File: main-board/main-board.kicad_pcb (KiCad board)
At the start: 2 copper layers, 180 x 111 mm, 57 parts, among them J1 INPUT, J2 NC1, J3 OUTPUT, J4 Conn_01x03_Pin, J5 COM, J6 Conn_01x03_Pin, SW1 SW_SPST, U1 ADA4898-2, U2 ADA4898-2, U3 AD633ANZ

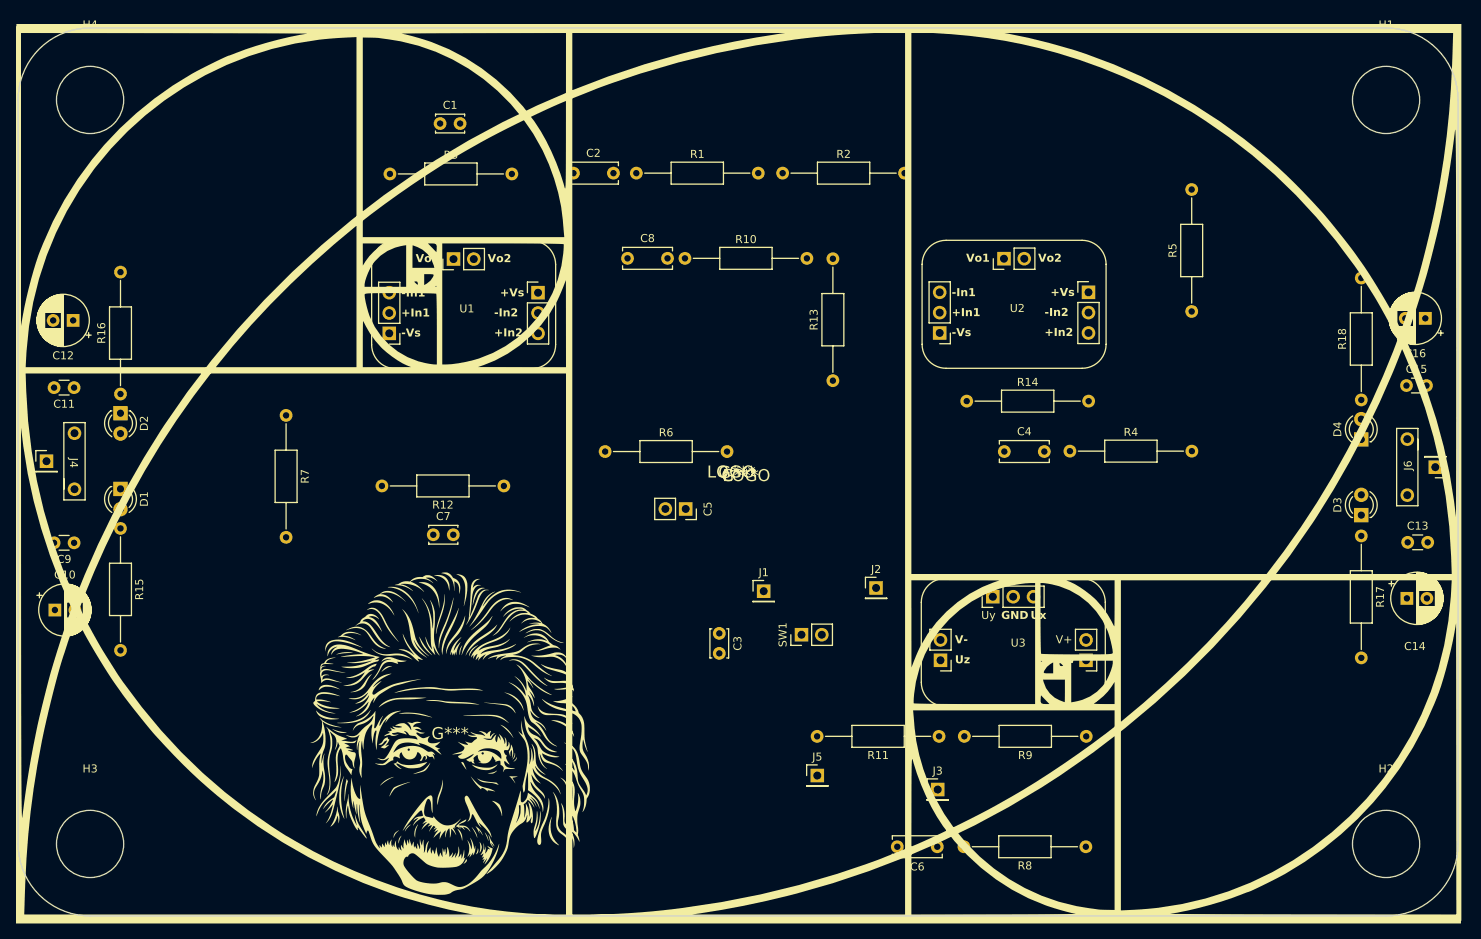
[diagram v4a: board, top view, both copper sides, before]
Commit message: Modifies main board layout components displacement
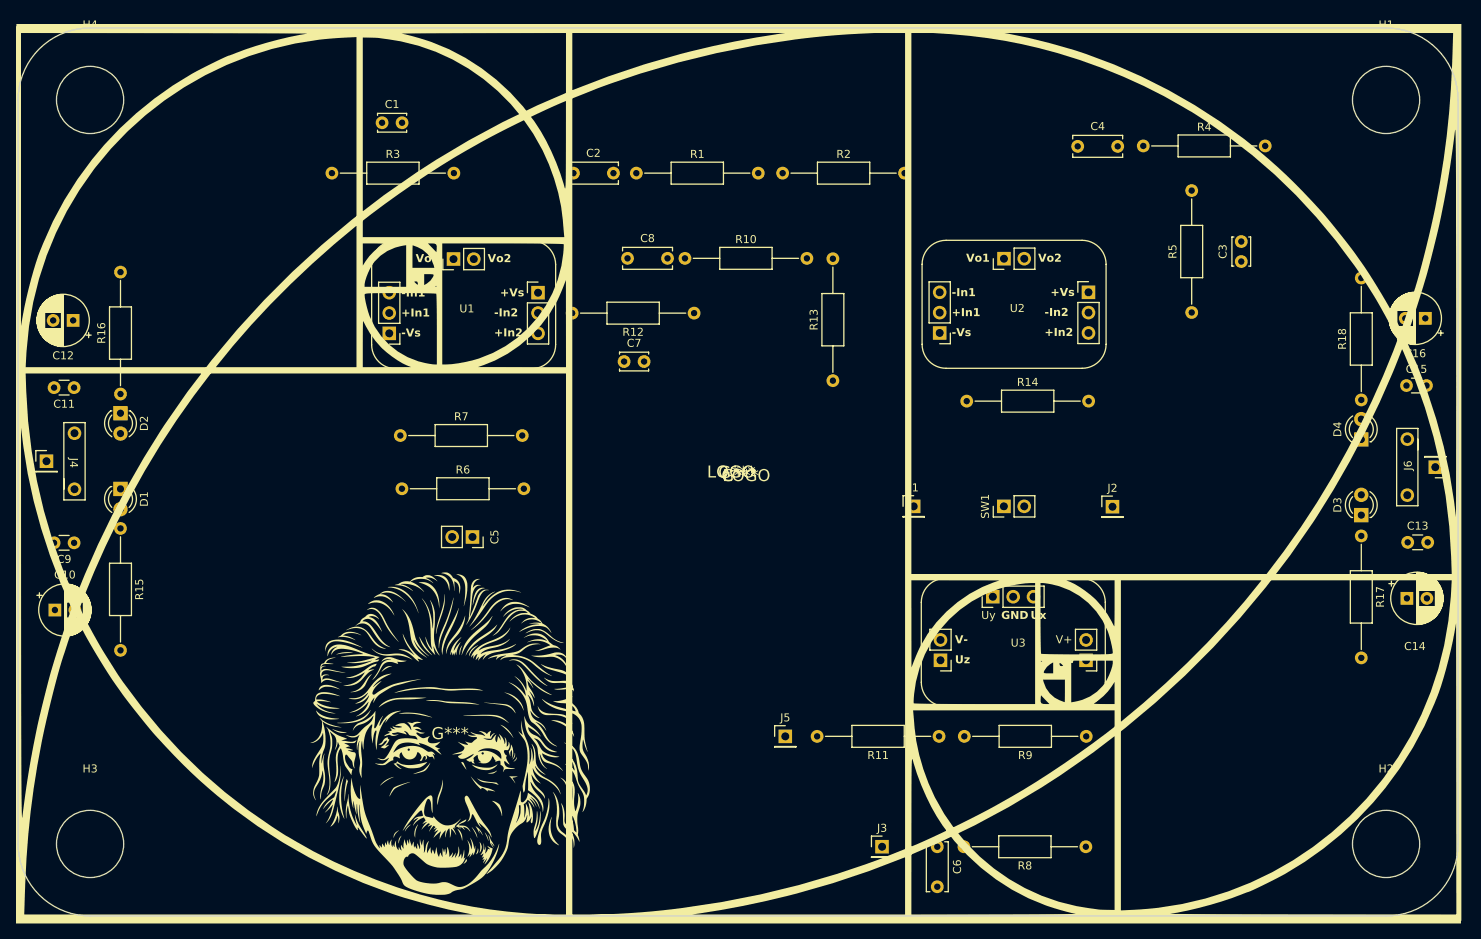
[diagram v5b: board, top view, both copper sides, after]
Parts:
- moved C3 80.1 mm to (212.9, 72.2), turned to 90 degrees
- moved R4 39.2 mm to (200.7, 57.8)
- moved C4 39.2 mm to (192.4, 57.8)
- moved C7 32.2 mm to (135.8, 84.7)
- moved R12 32.1 mm to (144.5, 78.7)
- moved J2 31.2 mm to (196.8, 102.8)
- moved SW1 30.0 mm to (183.2, 102.8)
- moved C5 26.9 mm to (116.8, 106.6)
- moved R6 25.8 mm to (108.0, 100.6)
- moved J1 21.5 mm to (171.9, 102.8)
- moved R7 14.5 mm to (107.8, 94.0), turned to 0 degrees
- moved J3 9.97 mm to (168.0, 145.3)
- moved C1 7.25 mm to (105.5, 54.9)
- moved R3 7.25 mm to (99.2, 61.1)
- moved J5 6.33 mm to (155.9, 131.6)
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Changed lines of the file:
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@@
   )
   (footprint "footprints:Switch" (layer "F.Cu")
-    (at 157.925 118.85 90)
+    (at 183.225 102.8 90)
     (property "Sheetfile" "main-board.kicad_sch")
     (property "Sheetname" "")
@@
   )
   (footprint "Capacitor_THT:C_Disc_D6.0mm_W2.5mm_P5.00mm" (layer "F.Cu")
-    (at 183.28 95.95)
+    (at 192.45 57.8)
     (descr "C, Disc series, Radial, pin pitch=5.00mm, , diameter*width=6*2.5mm^2, Capacitor, http://cdn-reichelt.de/documents/datenblatt/B300/DS_KERKO_TC.pdf")
     (tags "C Disc series Radial pin pitch 5.00mm  diameter 6mm width 2.5mm Capacitor")
@@
   )
   (footprint "Resistor_THT:R_Axial_DIN0207_L6.3mm_D2.5mm_P15.24mm_Horizontal" (layer "F.Cu")
-    (at 191.48 95.9)
+    (at 200.65 57.75)
     (descr "Resistor, Axial_DIN0207 series, Axial, Horizontal, pin pitch=15.24mm, 0.25W = 1/4W, length*diameter=6.3*2.5mm^2, http://cdn-reichelt.de/documents/datenblatt/B400/1_4W%23YAG.pdf")
     (tags "Resistor Axial_DIN0207 series Axial Horizontal pin pitch 15.24mm 0.25W = 1/4W length 6.3mm diameter 2.5mm")
@@
   )
   (footprint "Capacitor_THT:C_Disc_D3.4mm_W2.1mm_P2.50mm" (layer "F.Cu")
-    (at 112.75 54.95)
+    (at 105.5 54.85)
     (descr "C, Disc series, Radial, pin pitch=2.50mm, , diameter*width=3.4*2.1mm^2, Capacitor, http://www.vishay.com/docs/45233/krseries.pdf")
     (tags "C Disc series Radial pin pitch 2.50mm  diameter 3.4mm width 2.1mm Capacitor")
@@
   )
   (footprint "Connector_PinHeader_2.54mm:PinHeader_1x01_P2.54mm_Vertical" (layer "F.Cu")
-    (at 159.9 136.45)
+    (at 155.9 131.55)
     (descr "Through hole straight pin header, 1x01, 2.54mm pitch, single row")
     (tags "Through hole pin header THT 1x01 2.54mm single row")
@@
   )
   (footprint "Capacitor_THT:C_Disc_D6.0mm_W2.5mm_P5.00mm" (layer "F.Cu")
-    (at 174.9 145.35 180)
+    (at 174.9 145.35 -90)
     (descr "C, Disc series, Radial, pin pitch=5.00mm, , diameter*width=6*2.5mm^2, Capacitor, http://cdn-reichelt.de/documents/datenblatt/B300/DS_KERKO_TC.pdf")
     (tags "C Disc series Radial pin pitch 5.00mm  diameter 6mm width 2.5mm Capacitor")
@@
     (property "ki_keywords" "cap capacitor")
     (attr through_hole)
-    (fp_text reference "C6" (at 2.5 -2.5) (layer "F.SilkS")
+    (fp_text reference "C6" (at 2.5 -2.5 -270) (layer "F.SilkS")
         (effects (font (size 1 1) (thickness 0.15)))
     )
-    (fp_text value "10u" (at 2.5 2.5) (layer "F.Fab")
+    (fp_text value "10u" (at 2.5 2.5 -270) (layer "F.Fab")
         (effects (font (size 1 1) (thickness 0.15)))
     )
-    (fp_text user "${REFERENCE}" (at 2.5 0) (layer "F.Fab")
+    (fp_text user "${REFERENCE}" (at 2.5 0 -270) (layer "F.Fab")
         (effects (font (size 1 1) (thickness 0.15)))
     )
@@
     (fp_line (start 5.5 1.25) (end 5.5 -1.25)
       (stroke (width 0.1) (type solid)) (layer "F.Fab"))
-    (pad "1" thru_hole circle (at 0 0 180) (size 1.6 1.6) (drill 0.8) (layers "*.Cu" "*.Mask")
+    (pad "1" thru_hole circle (at 0 0 270) (size 1.6 1.6) (drill 0.8) (layers "*.Cu" "*.Mask")
       (net 8 "/w_out") (pintype "passive"))
-    (pad "2" thru_hole circle (at 5 0 180) (size 1.6 1.6) (drill 0.8) (layers "*.Cu" "*.Mask")
+    (pad "2" thru_hole circle (at 5 0 270) (size 1.6 1.6) (drill 0.8) (layers "*.Cu" "*.Mask")
       (net 9 "GND") (pintype "passive"))
     (model "${KICAD6_3DMODEL_DIR}/Capacitor_THT.3dshapes/C_Disc_D6.0mm_W2.5mm_P5.00mm.wrl"
@@
   )
   (footprint "Resistor_THT:R_Axial_DIN0207_L6.3mm_D2.5mm_P15.24mm_Horizontal" (layer "F.Cu")
-    (at 206.7 78.44 90)
+    (at 206.7 78.57 90)
     (descr "Resistor, Axial_DIN0207 series, Axial, Horizontal, pin pitch=15.24mm, 0.25W = 1/4W, length*diameter=6.3*2.5mm^2, http://cdn-reichelt.de/documents/datenblatt/B400/1_4W%23YAG.pdf")
     (tags "Resistor Axial_DIN0207 series Axial Horizontal pin pitch 15.24mm 0.25W = 1/4W length 6.3mm diameter 2.5mm")
@@
   )
   (footprint "footprints:CapacitorSocket" (layer "F.Cu")
-    (at 143.45 103.125 -90)
+    (at 116.8 106.625 -90)
     (property "Sheetfile" "main-board.kicad_sch")
     (property "Sheetname" "")
@@
   )
   (footprint "Connector_PinHeader_2.54mm:PinHeader_1x01_P2.54mm_Vertical" (layer "F.Cu")
-    (at 174.95 138.2)
+    (at 168 145.35)
     (descr "Through hole straight pin header, 1x01, 2.54mm pitch, single row")
     (tags "Through hole pin header THT 1x01 2.54mm single row")
@@
   )
   (footprint "Resistor_THT:R_Axial_DIN0207_L6.3mm_D2.5mm_P15.24mm_Horizontal" (layer "F.Cu")
-    (at 133.38 95.95)
+    (at 107.98 100.6)
     (descr "Resistor, Axial_DIN0207 series, Axial, Horizontal, pin pitch=15.24mm, 0.25W = 1/4W, length*diameter=6.3*2.5mm^2, http://cdn-reichelt.de/documents/datenblatt/B400/1_4W%23YAG.pdf")
     (tags "Resistor Axial_DIN0207 series Axial Horizontal pin pitch 15.24mm 0.25W = 1/4W length 6.3mm diameter 2.5mm")
@@
   )
   (footprint "Resistor_THT:R_Axial_DIN0207_L6.3mm_D2.5mm_P15.24mm_Horizontal" (layer "F.Cu")
-    (at 93.5 91.43 -90)
+    (at 107.78 93.95)
     (descr "Resistor, Axial_DIN0207 series, Axial, Horizontal, pin pitch=15.24mm, 0.25W = 1/4W, length*diameter=6.3*2.5mm^2, http://cdn-reichelt.de/documents/datenblatt/B400/1_4W%23YAG.pdf")
     (tags "Resistor Axial_DIN0207 series Axial Horizontal pin pitch 15.24mm 0.25W = 1/4W length 6.3mm diameter 2.5mm")
@@
     (property "ki_keywords" "R res resistor")
     (attr through_hole)
-    (fp_text reference "R7" (at 7.62 -2.37 90) (layer "F.SilkS")
+    (fp_text reference "R7" (at 7.62 -2.37) (layer "F.SilkS")
         (effects (font (size 1 1) (thickness 0.15)))
     )
-    (fp_text value "20" (at 7.62 2.37 90) (layer "F.Fab")
+    (fp_text value "20" (at 7.62 2.37) (layer "F.Fab")
         (effects (font (size 1 1) (thickness 0.15)))
     )
-    (fp_text user "${REFERENCE}" (at 7.62 0 90) (layer "F.Fab")
+    (fp_text user "${REFERENCE}" (at 7.62 0) (layer "F.Fab")
         (effects (font (size 1 1) (thickness 0.15)))
     )
@@
     (fp_line (start 15.24 0) (end 10.77 0)
       (stroke (width 0.1) (type solid)) (layer "F.Fab"))
-    (pad "1" thru_hole circle (at 0 0 270) (size 1.6 1.6) (drill 0.8) (layers "*.Cu" "*.Mask")
+    (pad "1" thru_hole circle (at 0 0) (size 1.6 1.6) (drill 0.8) (layers "*.Cu" "*.Mask")
       (net 1 "/w1") (pintype "passive"))
-    (pad "2" thru_hole oval (at 15.24 0 270) (size 1.6 1.6) (drill 0.8) (layers "*.Cu" "*.Mask")
+    (pad "2" thru_hole oval (at 15.24 0) (size 1.6 1.6) (drill 0.8) (layers "*.Cu" "*.Mask")
       (net 10 "/w2") (pintype "passive"))
     (model "${KICAD6_3DMODEL_DIR}/Resistor_THT.3dshapes/R_Axial_DIN0207_L6.3mm_D2.5mm_P15.24mm_Horizontal.wrl"
@@
   )
   (footprint "Resistor_THT:R_Axial_DIN0207_L6.3mm_D2.5mm_P15.24mm_Horizontal" (layer "F.Cu")
-    (at 120.72 100.25 180)
+    (at 144.5 78.65 180)
     (descr "Resistor, Axial_DIN0207 series, Axial, Horizontal, pin pitch=15.24mm, 0.25W = 1/4W, length*diameter=6.3*2.5mm^2, http://cdn-reichelt.de/documents/datenblatt/B400/1_4W%23YAG.pdf")
     (tags "Resistor Axial_DIN0207 series Axial Horizontal pin pitch 15.24mm 0.25W = 1/4W length 6.3mm diameter 2.5mm")
@@
   )
   (footprint "Resistor_THT:R_Axial_DIN0207_L6.3mm_D2.5mm_P15.24mm_Horizontal" (layer "F.Cu")
-    (at 106.48 61.25)
+    (at 99.23 61.15)
     (descr "Resistor, Axial_DIN0207 series, Axial, Horizontal, pin pitch=15.24mm, 0.25W = 1/4W, length*diameter=6.3*2.5mm^2, http://cdn-reichelt.de/documents/datenblatt/B400/1_4W%23YAG.pdf")
     (tags "Resistor Axial_DIN0207 series Axial Horizontal pin pitch 15.24mm 0.25W = 1/4W length 6.3mm diameter 2.5mm")
@@
   )
   (footprint "Capacitor_THT:C_Disc_D3.4mm_W2.1mm_P2.50mm" (layer "F.Cu")
-    (at 147.65 118.68 -90)
+    (at 212.9 72.2 90)
     (descr "C, Disc series, Radial, pin pitch=2.50mm, , diameter*width=3.4*2.1mm^2, Capacitor, http://www.vishay.com/docs/45233/krseries.pdf")
     (tags "C Disc series Radial pin pitch 2.50mm  diameter 3.4mm width 2.1mm Capacitor")
@@
     (fp_line (start 2.95 1.05) (end 2.95 -1.05)
       (stroke (width 0.1) (type solid)) (layer "F.Fab"))
-    (pad "1" thru_hole circle (at 0 0 270) (size 1.6 1.6) (drill 0.8) (layers "*.Cu" "*.Mask")
+    (pad "1" thru_hole circle (at 0 0 90) (size 1.6 1.6) (drill 0.8) (layers "*.Cu" "*.Mask")
       (net 26 "/w12") (pintype "passive"))
-    (pad "2" thru_hole circle (at 2.5 0 270) (size 1.6 1.6) (drill 0.8) (layers "*.Cu" "*.Mask")
+    (pad "2" thru_hole circle (at 2.5 0 90) (size 1.6 1.6) (drill 0.8) (layers "*.Cu" "*.Mask")
       (net 4 "/w_input") (pintype "passive"))
     (model "${KICAD6_3DMODEL_DIR}/Capacitor_THT.3dshapes/C_Disc_D3.4mm_W2.1mm_P2.50mm.wrl"
@@
   )
   (footprint "Capacitor_THT:C_Disc_D3.4mm_W2.1mm_P2.50mm" (layer "F.Cu")
-    (at 111.9 106.35)
+    (at 135.75 84.7)
     (descr "C, Disc series, Radial, pin pitch=2.50mm, , diameter*width=3.4*2.1mm^2, Capacitor, http://www.vishay.com/docs/45233/krseries.pdf")
     (tags "C Disc series Radial pin pitch 2.50mm  diameter 3.4mm width 2.1mm Capacitor")
@@
   )
   (footprint "Connector_PinHeader_2.54mm:PinHeader_1x01_P2.54mm_Vertical" (layer "F.Cu")
-    (at 153.2 113.4)
+    (at 171.95 102.8)
     (descr "Through hole straight pin header, 1x01, 2.54mm pitch, single row")
     (tags "Through hole pin header THT 1x01 2.54mm single row")
@@
   )
   (footprint "Connector_PinHeader_2.54mm:PinHeader_1x01_P2.54mm_Vertical" (layer "F.Cu")
-    (at 167.25 113)
+    (at 196.8 102.85)
     (descr "Through hole straight pin header, 1x01, 2.54mm pitch, single row")
     (tags "Through hole pin header THT 1x01 2.54mm single row")

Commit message: Starts routing the main board
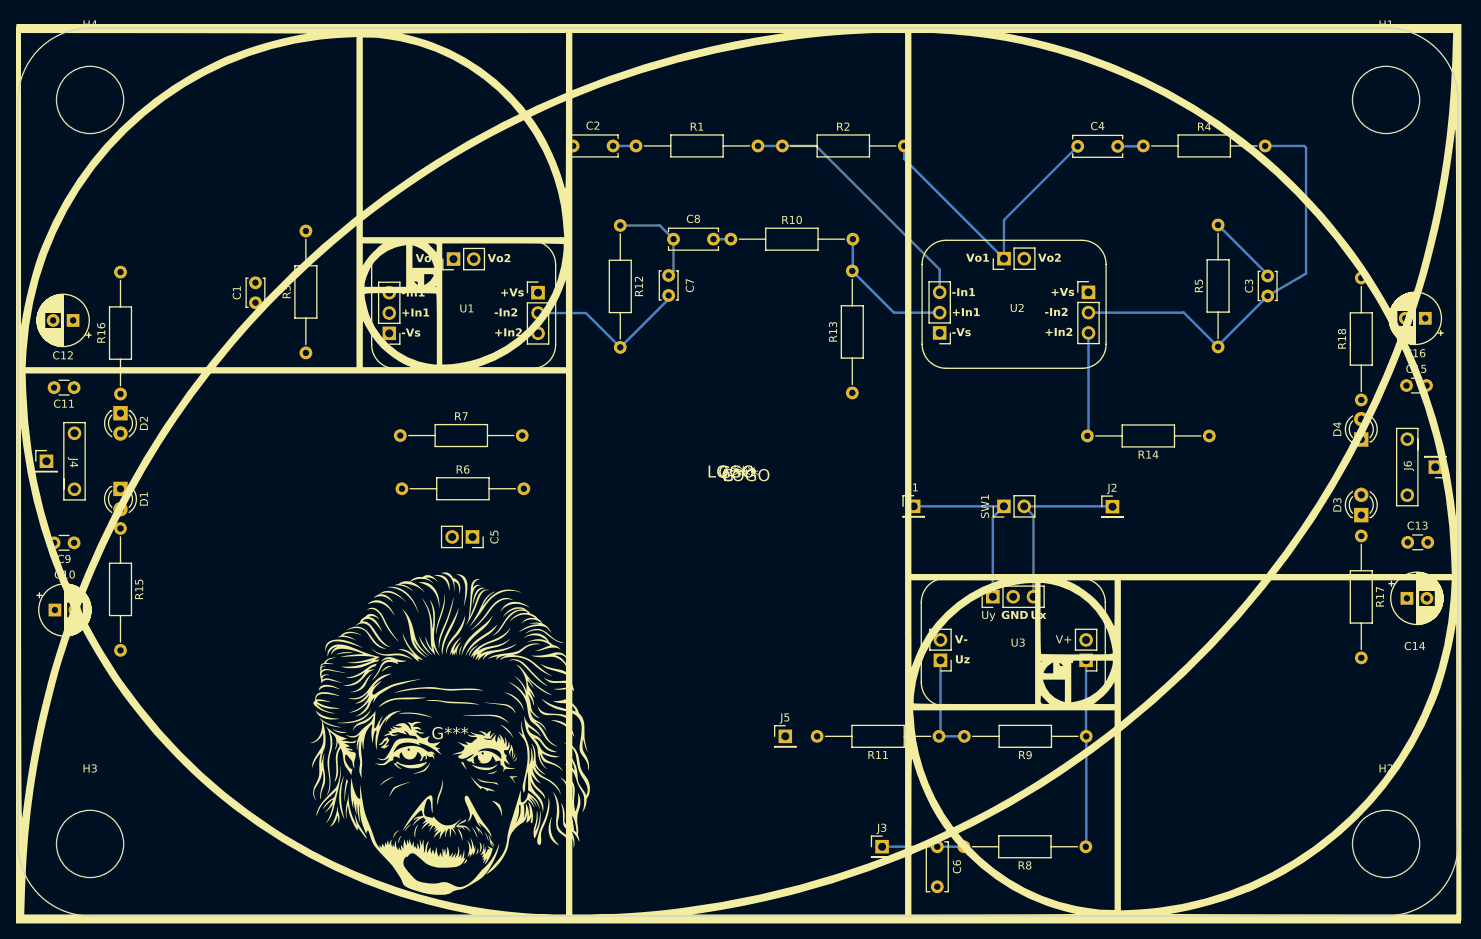
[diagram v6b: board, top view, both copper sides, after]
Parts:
- moved R14 30.6 mm to (208.9, 94.0), turned to 180 degrees
- moved C1 27.5 mm to (89.7, 77.3), turned to 90 degrees
- moved R3 22.7 mm to (96.0, 83.6), turned to 90 degrees
- moved R12 14.3 mm to (135.3, 67.7), turned to -90 degrees
- moved C7 9.97 mm to (141.3, 76.4), turned to 90 degrees
- moved C8 6.22 mm to (141.9, 69.4)
- moved R10 6.22 mm to (149.1, 69.4)
- moved R5 5.42 mm to (210.0, 82.9)
- moved C3 5.42 mm to (216.2, 76.5)
- moved C2 3.40 mm to (129.4, 57.8)
- moved R1 3.40 mm to (137.2, 57.8)
- moved R2 3.40 mm to (155.5, 57.8)
- moved R13 2.87 mm to (164.3, 88.6)
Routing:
- net /w12: track 0.00 -> 53.4 mm
- net /w10: track 0.00 -> 37.1 mm
- net /w_input: track 0.00 -> 32.1 mm
- net /w7: track 0.00 -> 32.0 mm
- net /w13: track 0.00 -> 23.3 mm
- net /w_nc: track 0.00 -> 22.8 mm
- net /w2: track 0.00 -> 21.1 mm
- net /w8: track 0.00 -> 17.1 mm
- net /w9: track 0.00 -> 12.9 mm
- net /w14: track 0.00 -> 12.7 mm
- net /w4: track 0.00 -> 12.1 mm
- net /w_out: track 0.00 -> 10.2 mm
- net /w11: track 0.00 -> 3.22 mm
- net /w5: track 0.00 -> 2.86 mm
- net /w6: track 0.00 -> 2.18 mm

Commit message: Finishes version Beta of the project
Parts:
- removed the G*** at (150.1, 98.5)
- removed the G*** at (150.1, 99.0)
- removed the G*** at (149.8, 98.5)
- removed the G*** at (150.2, 99.0)
- moved R14 25.2 mm to (183.9, 91.1), turned to 0 degrees
- moved C14 10.5 mm to (232.7, 124.8)
- moved C16 8.82 mm to (235.3, 70.5)
- moved C12 8.57 mm to (67.2, 71.0)
- moved C10 8.04 mm to (64.6, 123.8)
- moved C13 6.21 mm to (232.6, 113.4)
- moved C11 5.36 mm to (67.0, 82.6)
- moved C15 5.14 mm to (232.9, 82.6)
- moved R2 4.55 mm to (159.9, 59.0)
- moved R7 4.08 mm to (108.3, 89.9)
- moved C9 4.04 mm to (67.0, 111.4)
- moved R18 3.51 mm to (227.6, 86.0)
- moved R13 3.03 mm to (167.3, 88.6)
- moved R10 3.00 mm to (152.1, 69.4)
- moved R17 2.91 mm to (227.6, 109.4)
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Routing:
- net VEE: track 0.00 -> 139.5 mm
- net VDD: track 0.00 -> 110.2 mm, vias 0 -> 2
- net VCC: track 0.00 -> 99.1 mm, vias 0 -> 2
- net VSS: track 0.00 -> 70.1 mm
- net /w_input: track 32.1 -> 96.2 mm
- net /w3: track 0.00 -> 48.4 mm
- net /w1: track 0.00 -> 45.4 mm
- net /w_signal+: track 0.00 -> 38.0 mm
- net /w_signal-: track 0.00 -> 33.1 mm
- net /w4: track 12.1 -> 32.0 mm
- net /w2: track 21.1 -> 39.5 mm
- net /w12: track 53.4 -> 66.1 mm
- net /w10: track 37.1 -> 28.8 mm
- net /led_VDD: track 0.00 -> 5.76 mm
- net /led_VEE: track 0.00 -> 5.65 mm
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- added copper zone on B.Cu, net GND
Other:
- board text added: "C"
- board text added: "COM"
- board text added: "Einstein-Boltzmann Board"
- board text added: "GND"
- board text added: "IN"
- board text added: "NC"
- board text added: "OUT"
- board text added: "Original Design from: 5-th Experimental Physics Olympiad (2017) Adapted by: Carlos Veras (@CarlosCraveiro - 2024) GitHub: https://github.com/CarlosCraveiro/einstein-boltzmann"
- board text added: "V+"
- board text added: "V-"
